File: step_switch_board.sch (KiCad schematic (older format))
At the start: 74 parts, among them SW23 STEP1, SW24 STEP2, SW25 STEP3, SW26 STEP4, SW27 STEP5, SW28 STEP6, SW29 STEP7, SW30 STEP8, SW31 STEP9, SW32 STEP10, SW33 STEP11, SW34 STEP12, SW35 STEP13, SW36 STEP14, SW37 STEP15, SW38 STEP16, U38 74HC165, U39 74HC165, U40 74AC595, U41 74AC595

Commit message: ERC done, 7 warnings that check out
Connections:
- net at R468.1: now also D93.2 (A)
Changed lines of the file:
@@
 Connection ~ 15200 1825
 Wire Wire Line
-	14300 1375 14500 1375
+	14250 1375 14500 1375
 Wire Wire Line
 	14300 1825 14450 1825

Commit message: netlist exported, starting footprint assignment
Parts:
- C192, C193, C194, C195: footprint ~ -> MyModules:SM0603-C-JRL
- D73, D74, D75, D76, D77, D78, D79, D86, D87, D88, D89, D90, D91, D92, D93, D94: footprint (none) -> MyModules:3MM-LED-C1A2
- R451, R452, R453, R454, R455, R456, R457, R458, R459, R460, R461, R462, R463, R464, R465, R466, R467, R468, R469, R470, R471, R472, R473, R474, R475, R476, R477, R478, R479, R480, R481, R482, R483: footprint ~ -> (none)

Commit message: all parts assinged except MIDI jack
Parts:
- R451, R452, R453, R454, R455, R456, R457, R458, R459, R460, R461, R462, R463, R464, R465, R466, R467, R468, R469, R470, R471, R472, R473, R474, R475, R476, R477, R478, R479, R480, R481, R482, R483: footprint (none) -> MyModules:SM0603-R-JRL
- SW23, SW24, SW25, SW26, SW27, SW28, SW29, SW30, SW31, SW32, SW33, SW34, SW35, SW36, SW37, SW38: footprint (none) -> MyModules:BF-4050-OMRON
- TP20: footprint (none) -> MyModules:TEST_POINT_LOOP_4592
- U38, U39, U40, U41: footprint (none) -> Housings_SSOP:TSSOP-16_4.4x5mm_Pitch0.65mm

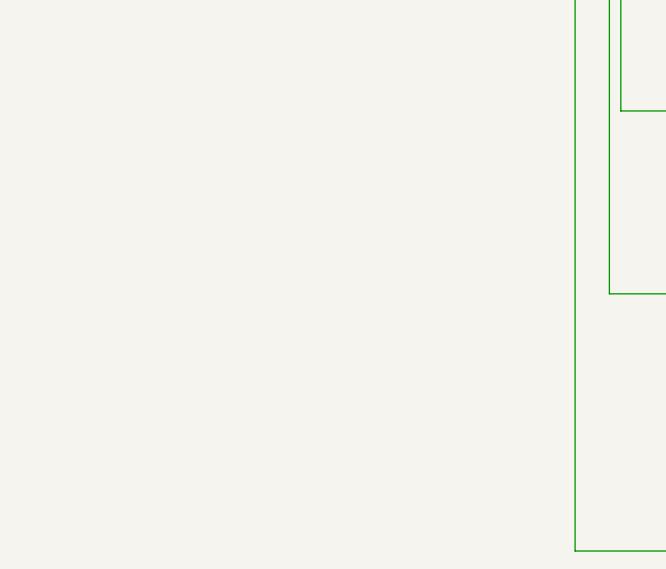
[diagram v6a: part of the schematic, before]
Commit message: added GH series low profile connector to connect step switch board to main board, added outline for step switch board, adjusted height of mainboard to 105 mm from 100 mm
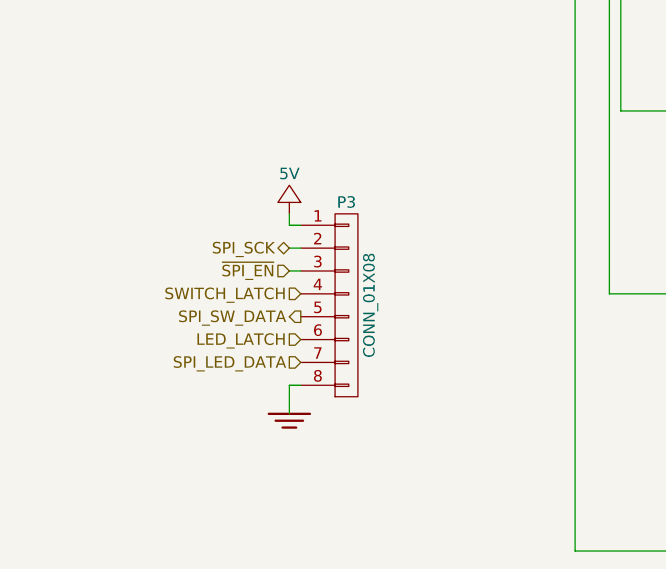
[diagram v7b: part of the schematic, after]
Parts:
- added P3: CONN_01X08, MyModules:GH-SIDE-8, symbol CONN_01X08
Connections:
- net +5V: now also P3.1 (P1)
- net GND: now also P3.8 (P8)
- net LED_LATCH: now also P3.6 (P6)
- net SPI_LED_DATA: now also P3.7 (P7)
- net SPI_SCK: now also P3.2 (P2)
- net SPI_SW_DATA: now also P3.5 (P5)
- net SWITCH_LATCH: now also P3.4 (P4)
- net ~SPI_EN: now also P3.3 (P3)
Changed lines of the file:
@@
 $EndComp
 $Comp
-L GND_E #PWR0496
+L GND_E #PWR0498
 U 1 1 569A130D
 P 7150 3775
-F 0 "#PWR0496" V 7150 3775 30  0001 C CNN
+F 0 "#PWR0498" V 7150 3775 30  0001 C CNN
 F 1 "GND_E" H 7150 3705 30  0001 C CNN
 F 2 "~" H 7150 3775 60  0000 C CNN
@@
 $EndComp
 $Comp
-L GND_E #PWR0497
+L GND_E #PWR0499
 U 1 1 569A1313
 P 6700 5775
-F 0 "#PWR0497" V 6700 5775 30  0001 C CNN
+F 0 "#PWR0499" V 6700 5775 30  0001 C CNN
 F 1 "GND_E" H 6700 5705 30  0001 C CNN
 F 2 "~" H 6700 5775 60  0000 C CNN
@@
 $EndComp
 $Comp
-L GND_E #PWR0498
+L GND_E #PWR0500
 U 1 1 569A1320
 P 8150 2275
-F 0 "#PWR0498" V 8150 2275 30  0001 C CNN
+F 0 "#PWR0500" V 8150 2275 30  0001 C CNN
 F 1 "GND_E" H 8150 2205 30  0001 C CNN
 F 2 "~" H 8150 2275 60  0000 C CNN
@@
 $EndComp
 $Comp
-L GND_E #PWR0499
+L GND_E #PWR0501
 U 1 1 569A132D
 P 8150 3075
-F 0 "#PWR0499" V 8150 3075 30  0001 C CNN
+F 0 "#PWR0501" V 8150 3075 30  0001 C CNN
 F 1 "GND_E" H 8150 3005 30  0001 C CNN
 F 2 "~" H 8150 3075 60  0000 C CNN
@@
 $EndComp
 $Comp
-L GND_E #PWR0500
+L GND_E #PWR0502
 U 1 1 569A133A
 P 8150 3875
-F 0 "#PWR0500" V 8150 3875 30  0001 C CNN
+F 0 "#PWR0502" V 8150 3875 30  0001 C CNN
 F 1 "GND_E" H 8150 3805 30  0001 C CNN
 F 2 "~" H 8150 3875 60  0000 C CNN
@@
 $EndComp
 $Comp
-L GND_E #PWR0501
+L GND_E #PWR0503
 U 1 1 569A1347
 P 8150 4675
-F 0 "#PWR0501" V 8150 4675 30  0001 C CNN
+F 0 "#PWR0503" V 8150 4675 30  0001 C CNN
 F 1 "GND_E" H 8150 4605 30  0001 C CNN
 F 2 "~" H 8150 4675 60  0000 C CNN
@@
 $EndComp
 $Comp
-L GND_E #PWR0502
+L GND_E #PWR0504
 U 1 1 569A1354
 P 8150 5475
-F 0 "#PWR0502" V 8150 5475 30  0001 C CNN
+F 0 "#PWR0504" V 8150 5475 30  0001 C CNN
 F 1 "GND_E" H 8150 5405 30  0001 C CNN
 F 2 "~" H 8150 5475 60  0000 C CNN
@@
 $EndComp
 $Comp
-L GND_E #PWR0503
+L GND_E #PWR0505
 U 1 1 569A1361
 P 8150 6275
-F 0 "#PWR0503" V 8150 6275 30  0001 C CNN
+F 0 "#PWR0505" V 8150 6275 30  0001 C CNN
 F 1 "GND_E" H 8150 6205 30  0001 C CNN
 F 2 "~" H 8150 6275 60  0000 C CNN
@@
 $EndComp
 $Comp
-L GND_E #PWR0504
+L GND_E #PWR0506
 U 1 1 569A136E
 P 8150 7075
-F 0 "#PWR0504" V 8150 7075 30  0001 C CNN
+F 0 "#PWR0506" V 8150 7075 30  0001 C CNN
 F 1 "GND_E" H 8150 7005 30  0001 C CNN
 F 2 "~" H 8150 7075 60  0000 C CNN
@@
 $EndComp
 $Comp
-L GND_E #PWR0505
+L GND_E #PWR0507
 U 1 1 569A137B
 P 8150 7875
-F 0 "#PWR0505" V 8150 7875 30  0001 C CNN
+F 0 "#PWR0507" V 8150 7875 30  0001 C CNN
 F 1 "GND_E" H 8150 7805 30  0001 C CNN
 F 2 "~" H 8150 7875 60  0000 C CNN
@@
 $EndComp
 $Comp
-L GND_E #PWR0506
+L GND_E #PWR0508
 U 1 1 569A1398
 P 2625 3775
-F 0 "#PWR0506" V 2625 3775 30  0001 C CNN
+F 0 "#PWR0508" V 2625 3775 30  0001 C CNN
 F 1 "GND_E" H 2625 3705 30  0001 C CNN
 F 2 "~" H 2625 3775 60  0000 C CNN
@@
 $EndComp
 $Comp
-L GND_E #PWR0507
+L GND_E #PWR0509
 U 1 1 569A139E
 P 2175 5775
-F 0 "#PWR0507" V 2175 5775 30  0001 C CNN
+F 0 "#PWR0509" V 2175 5775 30  0001 C CNN
 F 1 "GND_E" H 2175 5705 30  0001 C CNN
 F 2 "~" H 2175 5775 60  0000 C CNN
@@
 $EndComp
 $Comp
-L GND_E #PWR0508
+L GND_E #PWR0510
 U 1 1 569A13AB
 P 3625 2275
-F 0 "#PWR0508" V 3625 2275 30  0001 C CNN
+F 0 "#PWR0510" V 3625 2275 30  0001 C CNN
 F 1 "GND_E" H 3625 2205 30  0001 C CNN
 F 2 "~" H 3625 2275 60  0000 C CNN
@@
 $EndComp
 $Comp
-L GND_E #PWR0509
+L GND_E #PWR0511
 U 1 1 569A13B8
 P 3625 3075
-F 0 "#PWR0509" V 3625 3075 30  0001 C CNN
+F 0 "#PWR0511" V 3625 3075 30  0001 C CNN
 F 1 "GND_E" H 3625 3005 30  0001 C CNN
 F 2 "~" H 3625 3075 60  0000 C CNN
@@
 $EndComp
 $Comp
-L GND_E #PWR0510
+L GND_E #PWR0512
 U 1 1 569A13C5
 P 3625 3875
-F 0 "#PWR0510" V 3625 3875 30  0001 C CNN
+F 0 "#PWR0512" V 3625 3875 30  0001 C CNN
 F 1 "GND_E" H 3625 3805 30  0001 C CNN
 F 2 "~" H 3625 3875 60  0000 C CNN
@@
 $EndComp
 $Comp
-L GND_E #PWR0511
+L GND_E #PWR0513
 U 1 1 569A13D2
 P 3625 4675
-F 0 "#PWR0511" V 3625 4675 30  0001 C CNN
+F 0 "#PWR0513" V 3625 4675 30  0001 C CNN
 F 1 "GND_E" H 3625 4605 30  0001 C CNN
 F 2 "~" H 3625 4675 60  0000 C CNN
@@
 $EndComp
 $Comp
-L GND_E #PWR0512
+L GND_E #PWR0514
 U 1 1 569A13DF
 P 3625 5475
-F 0 "#PWR0512" V 3625 5475 30  0001 C CNN
+F 0 "#PWR0514" V 3625 5475 30  0001 C CNN
 F 1 "GND_E" H 3625 5405 30  0001 C CNN
 F 2 "~" H 3625 5475 60  0000 C CNN
@@
 $EndComp
 $Comp
-L GND_E #PWR0513
+L GND_E #PWR0515
 U 1 1 569A13EC
 P 3625 6275
-F 0 "#PWR0513" V 3625 6275 30  0001 C CNN
+F 0 "#PWR0515" V 3625 6275 30  0001 C CNN
 F 1 "GND_E" H 3625 6205 30  0001 C CNN
 F 2 "~" H 3625 6275 60  0000 C CNN
@@
 $EndComp
 $Comp
-L GND_E #PWR0514
+L GND_E #PWR0516
 U 1 1 569A13F9
 P 3625 7075
-F 0 "#PWR0514" V 3625 7075 30  0001 C CNN
+F 0 "#PWR0516" V 3625 7075 30  0001 C CNN
 F 1 "GND_E" H 3625 7005 30  0001 C CNN
 F 2 "~" H 3625 7075 60  0000 C CNN
@@
 $EndComp
 $Comp
-L GND_E #PWR0515
+L GND_E #PWR0517
 U 1 1 569A1406
 P 3625 7875
-F 0 "#PWR0515" V 3625 7875 30  0001 C CNN
+F 0 "#PWR0517" V 3625 7875 30  0001 C CNN
 F 1 "GND_E" H 3625 7805 30  0001 C CNN
 F 2 "~" H 3625 7875 60  0000 C CNN
@@
 $EndComp
 $Comp
-L 5V #PWR0516
+L 5V #PWR0518
 U 1 1 569C6046
 P 6700 3200
-F 0 "#PWR0516" H 6700 3050 50  0001 C CNN
+F 0 "#PWR0518" H 6700 3050 50  0001 C CNN
 F 1 "5V" H 6700 3375 50  0000 C CNN
 F 2 "" H 6700 3200 60  0000 C CNN
@@
 Connection ~ 6700 3275
 $Comp
-L 5V #PWR0517
+L 5V #PWR0519
 U 1 1 569C6C81
 P 2175 3200
-F 0 "#PWR0517" H 2175 3050 50  0001 C CNN
+F 0 "#PWR0519" H 2175 3050 50  0001 C CNN
 F 1 "5V" H 2175 3375 50  0000 C CNN
 F 2 "" H 2175 3200 60  0000 C CNN
@@
 Connection ~ 2175 3275
 $Comp
-L 5V #PWR0518
+L 5V #PWR0520
 U 1 1 56AA15B7
 P 4675 1525
-F 0 "#PWR0518" H 4675 1375 50  0001 C CNN
+F 0 "#PWR0520" H 4675 1375 50  0001 C CNN
 F 1 "5V" H 4675 1700 50  0000 C CNN
 F 2 "" H 4675 1525 60  0000 C CNN
@@
 $EndComp
 $Comp
-L 5V #PWR0519
+L 5V #PWR0521
 U 1 1 56AA548C
 P 9200 1525
-F 0 "#PWR0519" H 9200 1375 50  0001 C CNN
+F 0 "#PWR0521" H 9200 1375 50  0001 C CNN
 F 1 "5V" H 9200 1700 50  0000 C CNN
 F 2 "" H 9200 1525 60  0000 C CNN
@@
 GND
 $Comp
-L 5V #PWR0520
+L 5V #PWR0522
 U 1 1 56B2ED48
 P 1550 925
-F 0 "#PWR0520" H 1550 775 50  0001 C CNN
+F 0 "#PWR0522" H 1550 775 50  0001 C CNN
 F 1 "5V" H 1550 1100 50  0000 C CNN
 F 2 "" H 1550 925 60  0000 C CNN
@@
 	1550 1050 1550 925
 $Comp
-L GND_E #PWR0521
+L GND_E #PWR0523
 U 1 1 56B2F078
 P 1550 1350
-F 0 "#PWR0521" V 1550 1350 30  0001 C CNN
+F 0 "#PWR0523" V 1550 1350 30  0001 C CNN
 F 1 "GND_E" H 1550 1280 30  0001 C CNN
 F 2 "~" H 1550 1350 60  0000 C CNN
@@
 $EndComp
 $Comp
-L GND_E #PWR0522
+L GND_E #PWR0524
 U 1 1 56B96932
 P 12800 2125
-F 0 "#PWR0522" V 12800 2125 30  0001 C CNN
+F 0 "#PWR0524" V 12800 2125 30  0001 C CNN
 F 1 "GND_E" H 12800 2055 30  0001 C CNN
 F 2 "~" H 12800 2125 60  0000 C CNN
@@
 $EndComp
 $Comp
-L GND_E #PWR0523
+L GND_E #PWR0525
 U 1 1 56B9693F
 P 12350 3925
-F 0 "#PWR0523" V 12350 3925 30  0001 C CNN
+F 0 "#PWR0525" V 12350 3925 30  0001 C CNN
 F 1 "GND_E" H 12350 3855 30  0001 C CNN
 F 2 "~" H 12350 3925 60  0000 C CNN
@@
 $EndComp
 $Comp
-L GND_E #PWR0524
+L GND_E #PWR0526
 U 1 1 56B96985
 P 12800 5775
-F 0 "#PWR0524" V 12800 5775 30  0001 C CNN
+F 0 "#PWR0526" V 12800 5775 30  0001 C CNN
 F 1 "GND_E" H 12800 5705 30  0001 C CNN
 F 2 "~" H 12800 5775 60  0000 C CNN
@@
 $EndComp
 $Comp
-L GND_E #PWR0525
+L GND_E #PWR0527
 U 1 1 56B96992
 P 12350 7575
-F 0 "#PWR0525" V 12350 7575 30  0001 C CNN
+F 0 "#PWR0527" V 12350 7575 30  0001 C CNN
 F 1 "GND_E" H 12350 7505 30  0001 C CNN
 F 2 "~" H 12350 7575 60  0000 C CNN
@@
 $EndComp
 $Comp
-L GND_E #PWR0526
+L GND_E #PWR0528
 U 1 1 56B96999
 P 15200 8425
-F 0 "#PWR0526" V 15200 8425 30  0001 C CNN
+F 0 "#PWR0528" V 15200 8425 30  0001 C CNN
 F 1 "GND_E" H 15200 8355 30  0001 C CNN
 F 2 "~" H 15200 8425 60  0000 C CNN
@@
 $EndComp
 $Comp
-L GND_E #PWR0527
+L GND_E #PWR0529
 U 1 1 56B96A3F
 P 15200 4775
-F 0 "#PWR0527" V 15200 4775 30  0001 C CNN
+F 0 "#PWR0529" V 15200 4775 30  0001 C CNN
 F 1 "GND_E" H 15200 4705 30  0001 C CNN
 F 2 "~" H 15200 4775 60  0000 C CNN
@@
 $EndComp
 $Comp
-L 5V #PWR0528
+L 5V #PWR0530
 U 1 1 56B96A95
 P 12350 1550
-F 0 "#PWR0528" H 12350 1400 50  0001 C CNN
+F 0 "#PWR0530" H 12350 1400 50  0001 C CNN
 F 1 "5V" H 12350 1725 50  0000 C CNN
 F 2 "" H 12350 1550 60  0000 C CNN
@@
 Connection ~ 12350 1625
 $Comp
-L 5V #PWR0529
+L 5V #PWR0531
 U 1 1 56B96A9C
 P 12350 5225
-F 0 "#PWR0529" H 12350 5075 50  0001 C CNN
+F 0 "#PWR0531" H 12350 5075 50  0001 C CNN
 F 1 "5V" H 12350 5400 50  0000 C CNN
 F 2 "" H 12350 5225 60  0000 C CNN
@@
 Text Notes 5550 3725 0    60   ~ 0
 SPI SWITCH LATCH 2
+$Comp
+L CONN_01X08 P3
+U 1 1 56BE0A16
+P 2075 7425
+F 0 "P3" H 2075 7875 50  0000 C CNN
+F 1 "CONN_01X08" V 2175 7425 50  0000 C CNN
+F 2 "MyModules:GH-SIDE-8" H 2075 7425 60  0001 C CNN
+F 3 "" H 2075 7425 60  0000 C CNN
+	1    2075 7425
+	1    0    0    -1
+$EndComp
+$Comp
+L 5V #PWR0532
+U 1 1 56BE19E9
+P 1825 7025
+F 0 "#PWR0532" H 1825 6875 50  0001 C CNN
+F 1 "5V" H 1825 7200 50  0000 C CNN
+F 2 "" H 1825 7025 60  0000 C CNN
+F 3 "" H 1825 7025 60  0000 C CNN
+	1    1825 7025
+	1    0    0    -1
+$EndComp
+Wire Wire Line
+	1825 7025 1825 7075
+Wire Wire Line
+	1825 7075 1875 7075
+$Comp
+L GND_E #PWR0533
+U 1 1 56BE282C
+P 1825 7900
+F 0 "#PWR0533" V 1825 7900 30  0001 C CNN
+F 1 "GND_E" H 1825 7830 30  0001 C CNN
+F 2 "~" H 1825 7900 60  0000 C CNN
+F 3 "~" H 1825 7900 60  0000 C CNN
+	1    1825 7900
+	1    0    0    -1
+$EndComp
+Wire Wire Line
+	1875 7775 1825 7775
+Wire Wire Line
+	1825 7775 1825 7900
+Text HLabel 1825 7175 0    50   BiDi ~ 0
+SPI_SCK
+Wire Wire Line
+	1875 7175 1825 7175
+Text HLabel 1825 7275 0    50   Input ~ 0
+~SPI_EN
+Wire Wire Line
+	1825 7275 1875 7275
+Text HLabel 1875 7375 0    50   Input ~ 0
+SWITCH_LATCH
+Text HLabel 1875 7475 0    50   Output ~ 0
+SPI_SW_DATA
+Text HLabel 1875 7675 0    50   Input ~ 0
+SPI_LED_DATA
+Text HLabel 1875 7575 0    50   Input ~ 0
+LED_LATCH
 $EndSCHEMATC
